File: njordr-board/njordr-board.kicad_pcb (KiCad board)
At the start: 4 copper layers, 88 x 80 mm, 132 parts, among them IC101 DRV8300DPWR, IC2 GS8054, IC3 TMUX741x, J1 Conn_01x06, J2 Conn_01x06, J3 Conn_01x06, Q101 2N7002, Q102 2N7002, Q201 2N7002, Q202 2N7002, Q301 2N7002, Q302 2N7002, T1 TestPoint, T10 TestPoint, T101 TestPoint, T102 TestPoint, T103 TestPoint, T104 TestPoint, T105 TestPoint, T106 TestPoint, T107 TestPoint, T11 TestPoint, T2 TestPoint, T201 TestPoint, T202 TestPoint, T203 TestPoint, T204 TestPoint, T205 TestPoint, T206 TestPoint, T207 TestPoint, T3 TestPoint, T301 TestPoint, T302 TestPoint, T303 TestPoint, T304 TestPoint, T305 TestPoint, T306 TestPoint, T307 TestPoint, T4 TestPoint, T9 TestPoint, U2 MT3608, U3 REF3012, U7 LM393

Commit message: board: Improve board markings
- rotate reference labels
- add connector description
- add logo
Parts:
- moved C29 0.08 mm to (138.5, 87.0)
- moved R21 0.08 mm to (103.8, 105.3)
- moved C28 0.08 mm to (127.5, 71.3)
- moved C2 0.08 mm to (133.2, 88.5)
- moved C20 0.08 mm to (105.1, 114.6)
- moved C30 0.08 mm to (94.0, 85.7)
- moved R201 0.08 mm to (114.9, 70.1)
- moved ST101 0.08 mm to (128.9, 114.0)
- moved T307 0.08 mm to (142.1, 67.1)
- moved C17 0.08 mm to (102.1, 90.6)
- moved IC3 0.08 mm to (107.0, 96.6)
- moved C104 0.08 mm to (132.9, 101.7)
- moved C306 0.08 mm to (154.6, 77.2)
- moved C31 0.08 mm to (94.9, 87.3)
- moved R20 0.08 mm to (105.5, 108.3)
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- renumbered IC101 to IC1
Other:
- board text added: "NJORDR-BOARD 251025 JKR"

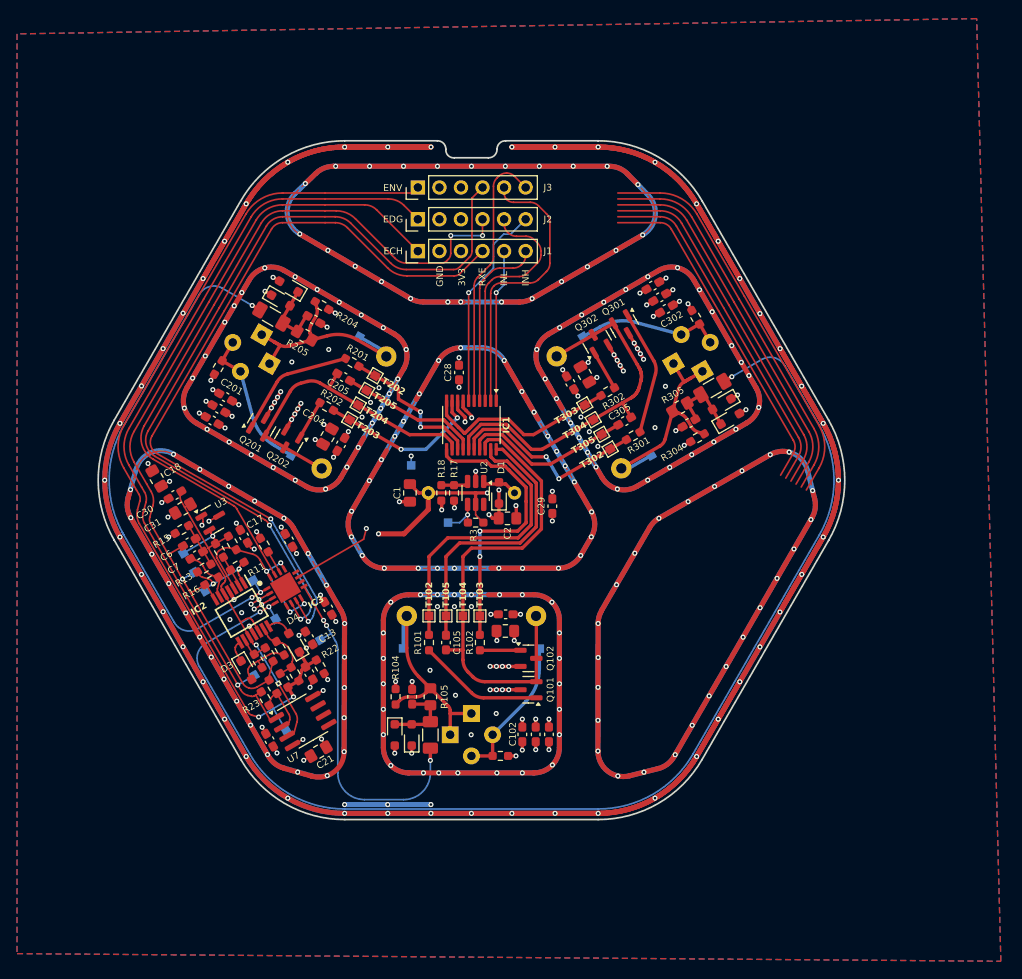
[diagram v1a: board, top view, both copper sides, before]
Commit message: board: Use lower resistor values for the envelope detector
- try to lower impedance to have higher stability
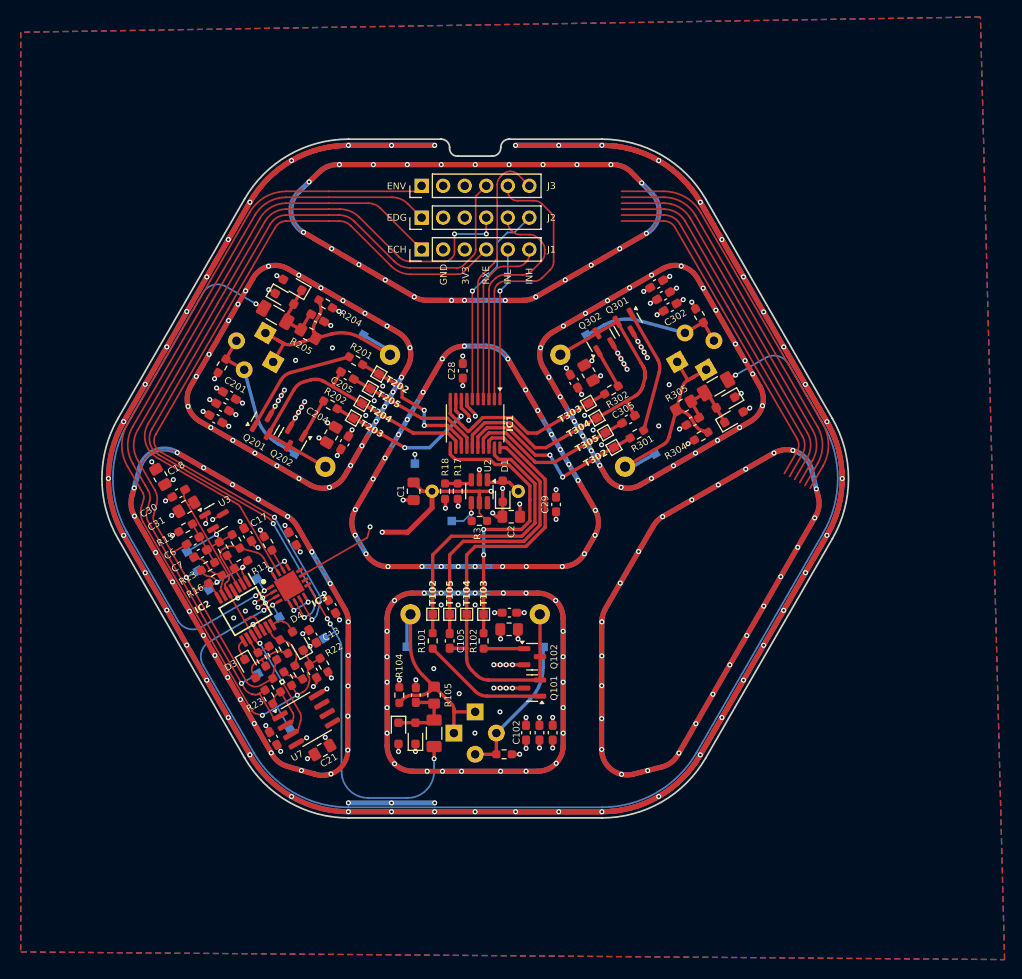
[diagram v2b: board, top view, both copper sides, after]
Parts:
- R19: value 20k -> 2k
- R21: value 10k -> 1k
- R24: value 30k -> 3k
- R25, R26: value 120k -> 3k
- moved T205 0.48 mm to (117.0, 73.2)
- moved T202 0.48 mm to (118.0, 71.5)
- moved D201 0.48 mm to (107.8, 61.0)
- moved C103 0.48 mm to (124.5, 113.8)
- moved C105 0.48 mm to (126.4, 102.9)
- moved C18 0.48 mm to (92.3, 83.6)
- moved C202 0.48 mm to (99.6, 75.4)
- moved C204 0.48 mm to (112.4, 78.6)
- moved L301 0.48 mm to (139.4, 69.2)
- moved R15 0.48 mm to (95.2, 89.6)
- moved T1 0.48 mm to (96.7, 94.6)
- moved C104 0.48 mm to (133.4, 101.6)
- moved C2 0.48 mm to (133.6, 88.3)
- moved IC2 0.48 mm to (102.3, 99.4)
- moved Q202 0.48 mm to (107.8, 79.1)
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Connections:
- R25 pad 1: /ENVELOPE -> Net-(R25-Pad1)
- R26 pad 2: Net-(IC2D--) -> Net-(R25-Pad1)
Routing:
- net Net-(R25-Pad1): track 0.00 -> 2.57 mm
- net Net-(IC2D--): track 8.25 -> 6.75 mm
- net /ENVELOPE: track 58.5 -> 59.5 mm

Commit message: njordr-board: Use updated library symbols and packages
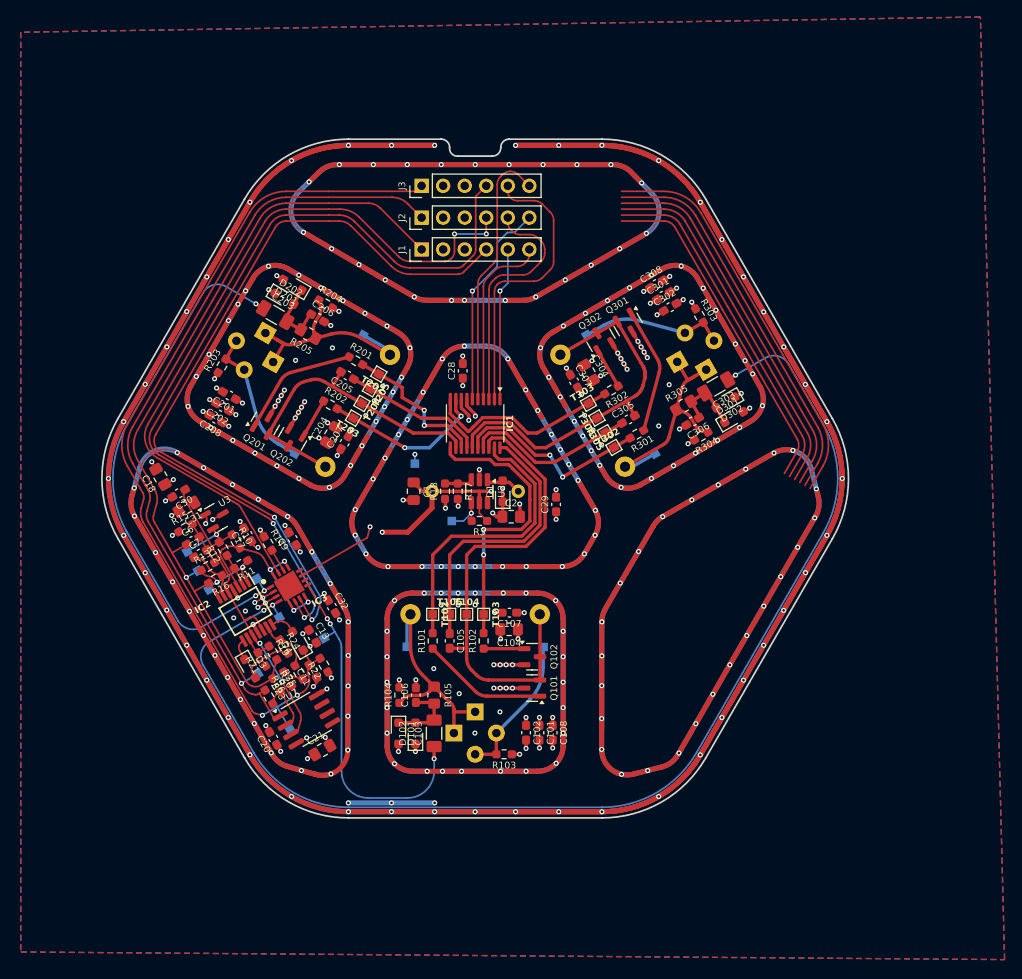
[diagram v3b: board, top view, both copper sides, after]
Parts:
- C1, C104, C18, C2, C204, C21, C304, C31: footprint njordr:C_0805_2012Metric_Pad1.18x1.45mm_HandSolder -> njordr:C-0805-HandSolder
- C101, C102, C105, C106, C107, C108, C11, C13, C17, C20, C201, C202, C205, C206, C207, C208, C28, C29, C30, C301, C302, C305, C306, C307, C308, C32, C6, C7, C9: footprint njordr:C_0603_1608Metric_Pad1.08x0.95mm_HandSolder -> njordr:C-0603-HandSolder
- C103, C203, C303: footprint njordr:C_1206_3216Metric_Pad1.33x1.80mm_HandSolder -> njordr:C-1206-HandSolder
- D1, D101, D102, D201, D202, D3, D301, D302, D4: footprint njordr:D_SOD-323_HandSoldering -> njordr:D-SOD-323-HandSolder
- J1, J2, J3: footprint njordr:PinHeader_1x06_P2.54mm_Vertical -> njordr:PinHeader-1x06-P2.54mm-Vertical
- L1: footprint njordr:L_Axial_L7.0mm_D3.3mm_P10.16mm_Horizontal_Fastron_MICC -> njordr:L-Axial-L7.0-D3.3mm-P10.16
- L101, L201, L301: footprint njordr:L_Axial_L12.0mm_D5.0mm_P15.24mm_Horizontal_Fastron_MISC -> njordr:L-Axial-L12.0-D5.0-P15.24
- R10, R101, R102, R103, R104, R11, R12, R13, R14, R15, R16, R17, R18, R19, R20, R201, R202, R203, R204, R21, R22, R23, R24, R25, R26, R3, R301, R302, R303, R304: footprint njordr:R_0603_1608Metric_Pad0.98x0.95mm_HandSolder -> njordr:R-0603-HandSolder
- R105, R205, R305: footprint njordr:R_0805_2012Metric_Pad1.20x1.40mm_HandSolder -> njordr:R-0805-HandSolder
- ST101, ST201, ST301: footprint njordr:Buzzer_D14mm_H9mm_P5mm -> njordr:CUSA-TR65-065-2200-TH68
- T1, T10, T101, T102, T103, T104, T105, T106, T107, T11, T2, T201, T202, T203, T204, T205, T206, T207, T3, T301, T302, T303, T304, T305, T306, T307, T4, T9: footprint njordr:TestPoint_Pad_1.0x1.0mm -> njordr:TestPoint-Pad-1.0x1.0
- U2: footprint njordr:SOT-23-6_Handsoldering -> njordr:SOT-23-6-HandSolder
- U7: footprint njordr:SOIC-8_3.9x4.9mm_P1.27mm -> njordr:SOIC-8-3.9x4.9-P1.27
